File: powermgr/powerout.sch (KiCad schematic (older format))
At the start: 14 parts, among them IC2 AP24x1, IC3 AP24x1, IC4 AP24x1, IC5 AP24x1, IC6 AP24x1, IC7 AP24x1, IC8 AP24x1, IC9 AP24x1, J3 CONN_01X02, J4 CONN_01X02, P1 CONN_01X16

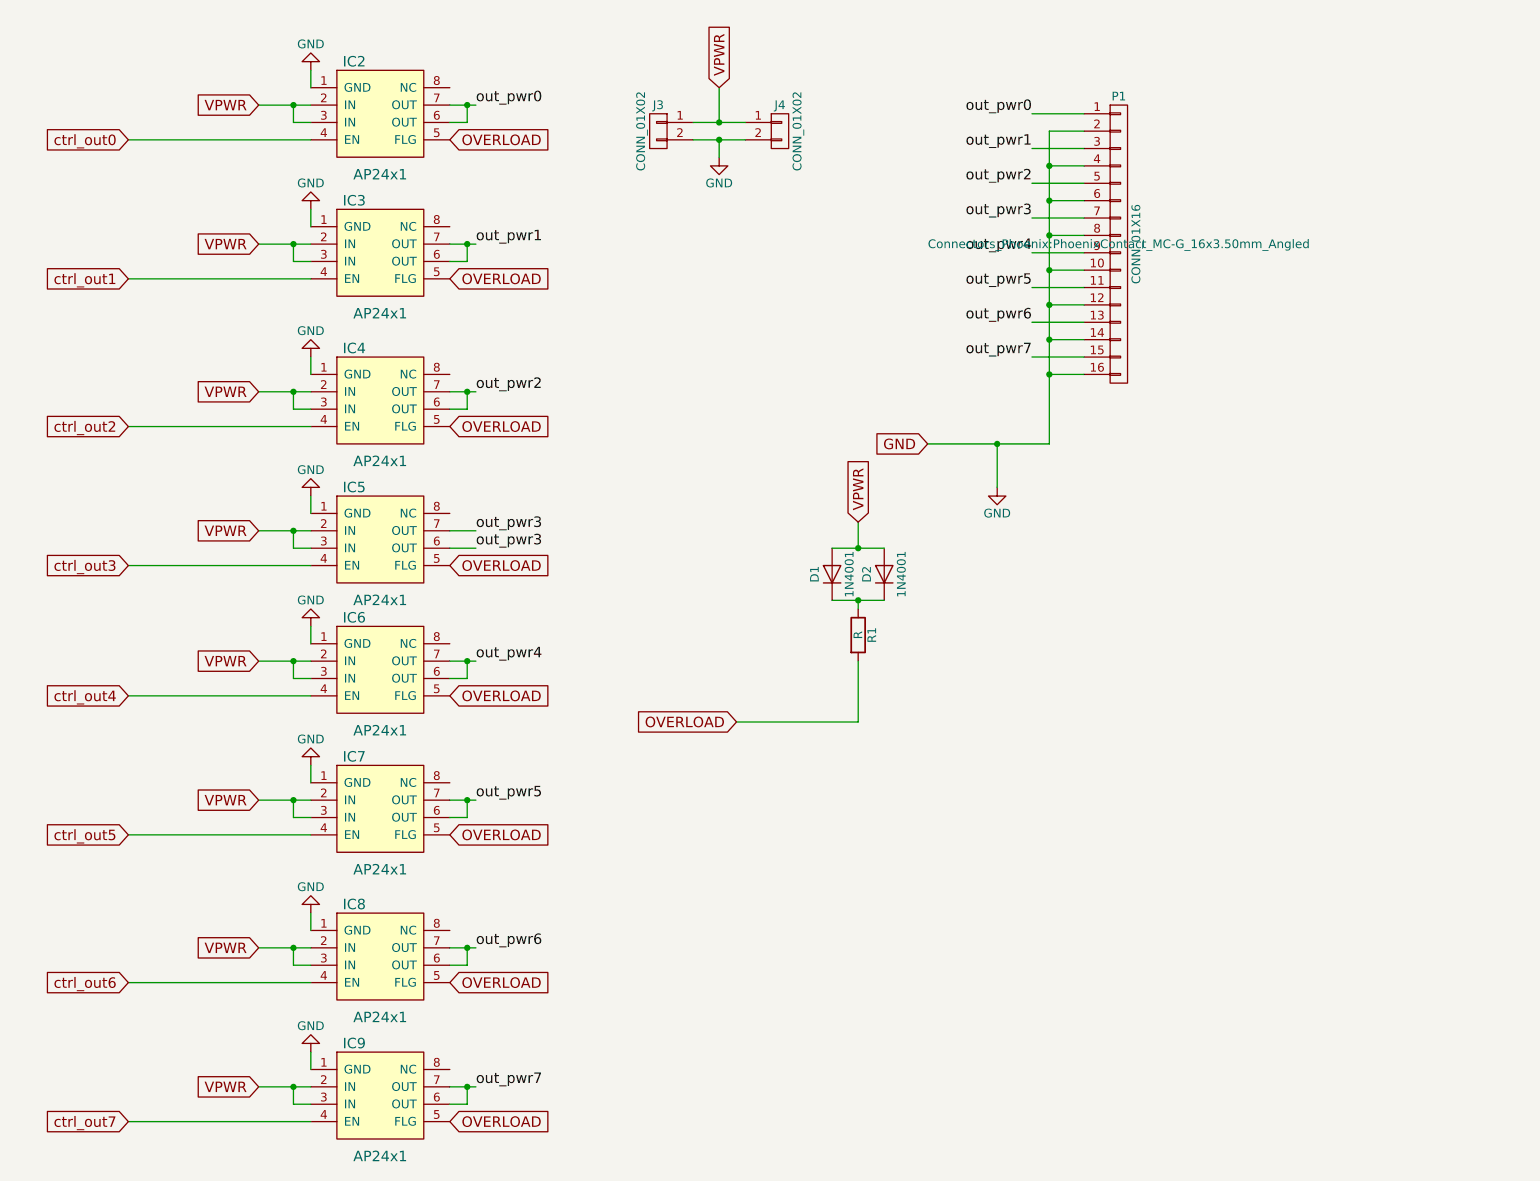
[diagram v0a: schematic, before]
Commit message: add LEDs and pulldowns
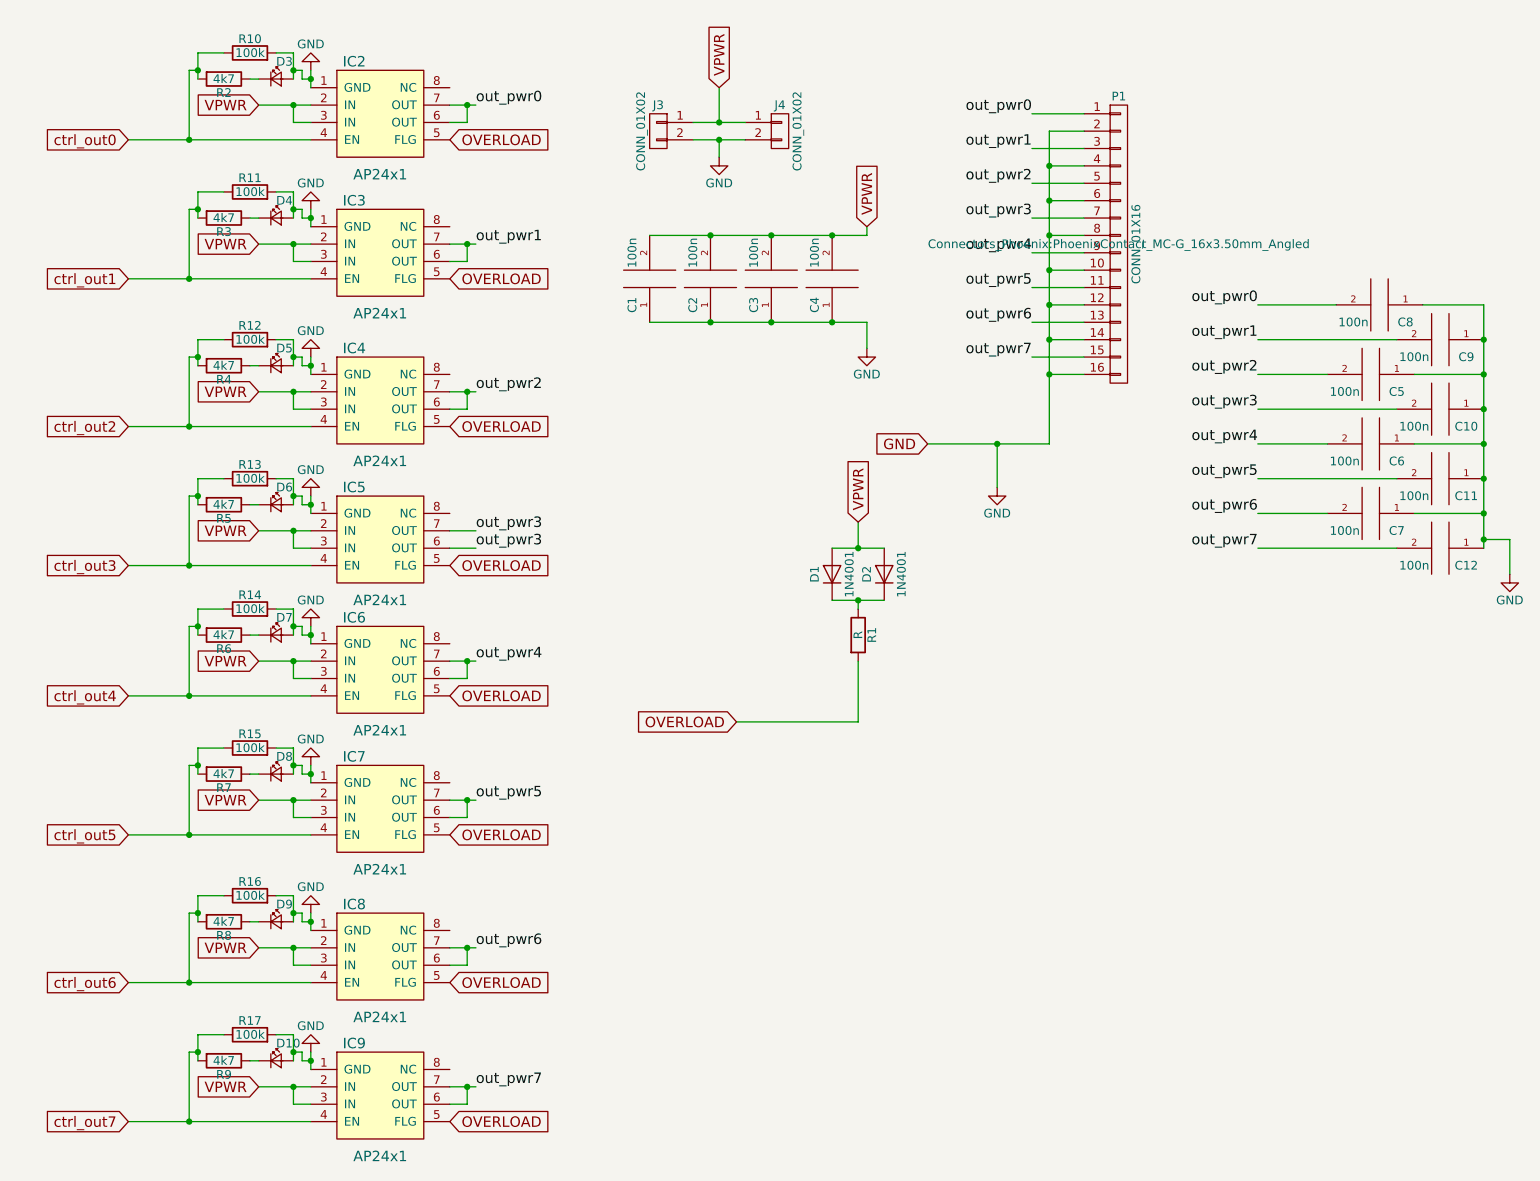
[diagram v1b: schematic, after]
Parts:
- added C1, C10, C11, C12, C2, C3, C4, C5, C6, C7, C8, C9: 100n, Capacitors_SMD:C_0805_HandSoldering, symbol CAP
- added D10, D3, D4, D5, D6, D7, D8, D9: LED_Small, LEDs:LED_0805, symbol LED_Small
- added R10, R11, R12, R13, R14, R15, R16, R17: 100k, Resistors_SMD:R_0805_HandSoldering, symbol R
- added R2, R3, R4, R5, R6, R7, R8, R9: 4k7, Resistors_SMD:R_0805_HandSoldering, symbol R
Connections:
- net GND: now also C1.1, C10.1, C11.1, C12.1, C2.1, C3.1, C4.1, C5.1, C6.1, C7.1, C8.1, C9.1, D10.2 (A), D3.2 (A), D4.2 (A), D5.2 (A), D6.2 (A), D7.2 (A), D8.2 (A), D9.2 (A), R10.2, R11.2, R12.2, R13.2, R14.2, R15.2, R16.2, R17.2
- net VPWR: now also C1.2, C2.2, C3.2, C4.2
- net ctrl_out0: now also R10.1, R2.2
- net ctrl_out1: now also R11.1, R3.2
- net ctrl_out2: now also R12.1, R4.2
- net ctrl_out3: now also R13.1, R5.2
- net ctrl_out4: now also R14.1, R6.2
- net ctrl_out5: now also R15.1, R7.2
- net ctrl_out6: now also R16.1, R8.2
- net ctrl_out7: now also R17.1, R9.2
- net out_pwr0: now also C8.2
- net out_pwr1: now also C9.2
- net out_pwr2: now also C5.2
- net out_pwr3: now also C10.2
- net out_pwr4: now also C6.2
- net out_pwr5: now also C11.2
- net out_pwr6: now also C7.2
- net out_pwr7: now also C12.2
- new net: D5.1 (K), R4.1
- new net: D4.1 (K), R3.1
- new net: D3.1 (K), R2.1
- new net: D6.1 (K), R5.1
- new net: D7.1 (K), R6.1
- new net: D8.1 (K), R7.1
- new net: D9.1 (K), R8.1
- new net: D10.1 (K), R9.1

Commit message: so-8 version, I bought wrong part number..
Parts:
- IC2, IC3, IC4, IC5, IC6, IC7, IC8, IC9: footprint Housings_SSOP:MSOP-8_3x3mm_Pitch0.65mm -> Housings_SOIC:SOIC-8_3.9x4.9mm_Pitch1.27mm
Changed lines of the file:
@@
 F 0 "IC2" H 2950 1250 60  0000 C CNN
 F 1 "AP24x1" H 3100 600 60  0000 C CNN
-F 2 "Housings_SSOP:MSOP-8_3x3mm_Pitch0.65mm" H 3150 900 60  0001 C CNN
+F 2 "Housings_SOIC:SOIC-8_3.9x4.9mm_Pitch1.27mm" H 3150 900 60  0001 C CNN
 F 3 "" H 3150 900 60  0000 C CNN
 F 4 "Diodes Incorporated" H 3100 500 60  0001 C CNN "Manufacturer"
@@
 F 0 "IC3" H 2950 2050 60  0000 C CNN
 F 1 "AP24x1" H 3100 1400 60  0000 C CNN
-F 2 "Housings_SSOP:MSOP-8_3x3mm_Pitch0.65mm" H 3150 1700 60  0001 C CNN
+F 2 "Housings_SOIC:SOIC-8_3.9x4.9mm_Pitch1.27mm" H 3150 1700 60  0001 C CNN
 F 3 "" H 3150 1700 60  0000 C CNN
 F 4 "Diodes Incorporated" H 3100 1300 60  0001 C CNN "Manufacturer"
@@
 F 0 "IC4" H 2950 2900 60  0000 C CNN
 F 1 "AP24x1" H 3100 2250 60  0000 C CNN
-F 2 "Housings_SSOP:MSOP-8_3x3mm_Pitch0.65mm" H 3150 2550 60  0001 C CNN
+F 2 "Housings_SOIC:SOIC-8_3.9x4.9mm_Pitch1.27mm" H 3150 2550 60  0001 C CNN
 F 3 "" H 3150 2550 60  0000 C CNN
 F 4 "Diodes Incorporated" H 3100 2150 60  0001 C CNN "Manufacturer"
@@
 F 0 "IC5" H 2950 3700 60  0000 C CNN
 F 1 "AP24x1" H 3100 3050 60  0000 C CNN
-F 2 "Housings_SSOP:MSOP-8_3x3mm_Pitch0.65mm" H 3150 3350 60  0001 C CNN
+F 2 "Housings_SOIC:SOIC-8_3.9x4.9mm_Pitch1.27mm" H 3150 3350 60  0001 C CNN
 F 3 "" H 3150 3350 60  0000 C CNN
 F 4 "Diodes Incorporated" H 3100 2950 60  0001 C CNN "Manufacturer"
@@
 F 0 "IC6" H 2950 4450 60  0000 C CNN
 F 1 "AP24x1" H 3100 3800 60  0000 C CNN
-F 2 "Housings_SSOP:MSOP-8_3x3mm_Pitch0.65mm" H 3150 4100 60  0001 C CNN
+F 2 "Housings_SOIC:SOIC-8_3.9x4.9mm_Pitch1.27mm" H 3150 4100 60  0001 C CNN
 F 3 "" H 3150 4100 60  0000 C CNN
 F 4 "Diodes Incorporated" H 3100 3700 60  0001 C CNN "Manufacturer"
@@
 F 0 "IC7" H 2950 5250 60  0000 C CNN
 F 1 "AP24x1" H 3100 4600 60  0000 C CNN
-F 2 "Housings_SSOP:MSOP-8_3x3mm_Pitch0.65mm" H 3150 4900 60  0001 C CNN
+F 2 "Housings_SOIC:SOIC-8_3.9x4.9mm_Pitch1.27mm" H 3150 4900 60  0001 C CNN
 F 3 "" H 3150 4900 60  0000 C CNN
 F 4 "Diodes Incorporated" H 3100 4500 60  0001 C CNN "Manufacturer"
@@
 F 0 "IC8" H 2950 6100 60  0000 C CNN
 F 1 "AP24x1" H 3100 5450 60  0000 C CNN
-F 2 "Housings_SSOP:MSOP-8_3x3mm_Pitch0.65mm" H 3150 5750 60  0001 C CNN
+F 2 "Housings_SOIC:SOIC-8_3.9x4.9mm_Pitch1.27mm" H 3150 5750 60  0001 C CNN
 F 3 "" H 3150 5750 60  0000 C CNN
 F 4 "Diodes Incorporated" H 3100 5350 60  0001 C CNN "Manufacturer"
@@
 F 0 "IC9" H 2950 6900 60  0000 C CNN
 F 1 "AP24x1" H 3100 6250 60  0000 C CNN
-F 2 "Housings_SSOP:MSOP-8_3x3mm_Pitch0.65mm" H 3150 6550 60  0001 C CNN
+F 2 "Housings_SOIC:SOIC-8_3.9x4.9mm_Pitch1.27mm" H 3150 6550 60  0001 C CNN
 F 3 "" H 3150 6550 60  0000 C CNN
 F 4 "Diodes Incorporated" H 3100 6150 60  0001 C CNN "Manufacturer"

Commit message: fixups and text
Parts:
- P1: value CONN_01X16 -> PWR_OUT
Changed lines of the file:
@@
 P 7350 1700
 F 0 "P1" H 7350 2550 50  0000 C CNN
-F 1 "CONN_01X16" V 7450 1700 50  0000 C CNN
+F 1 "PWR_OUT" V 7450 1700 50  0000 C CNN
 F 2 "Connectors_Phoenix:PhoenixContact_MC-G_16x3.50mm_Angled" H 7350 1700 50  0000 C CNN
 F 3 "" H 7350 1700 50  0000 C CNN
@@
 VPWR
 $Comp
-L GND #PWR07
+L GND #PWR09
 U 1 1 5908E164
 P 6650 3100
-F 0 "#PWR07" H 6650 2850 50  0001 C CNN
+F 0 "#PWR09" H 6650 2850 50  0001 C CNN
 F 1 "GND" H 6650 2950 50  0000 C CNN
 F 2 "" H 6650 3100 50  0001 C CNN
@@
 $EndComp
 $Comp
-L GND #PWR08
+L GND #PWR010
 U 1 1 5908E298
 P 2700 3150
-F 0 "#PWR08" H 2700 2900 50  0001 C CNN
+F 0 "#PWR010" H 2700 2900 50  0001 C CNN
 F 1 "GND" H 2700 3000 50  0000 C CNN
 F 2 "" H 2700 3150 50  0001 C CNN
@@
 $EndComp
 $Comp
-L GND #PWR09
+L GND #PWR011
 U 1 1 5908E35C
 P 2700 3900
-F 0 "#PWR09" H 2700 3650 50  0001 C CNN
+F 0 "#PWR011" H 2700 3650 50  0001 C CNN
 F 1 "GND" H 2700 3750 50  0000 C CNN
 F 2 "" H 2700 3900 50  0001 C CNN
@@
 $EndComp
 $Comp
-L GND #PWR010
+L GND #PWR012
 U 1 1 5908E706
 P 2700 4700
-F 0 "#PWR010" H 2700 4450 50  0001 C CNN
+F 0 "#PWR012" H 2700 4450 50  0001 C CNN
 F 1 "GND" H 2700 4550 50  0000 C CNN
 F 2 "" H 2700 4700 50  0001 C CNN
@@
 $EndComp
 $Comp
-L GND #PWR011
+L GND #PWR013
 U 1 1 5908E72C
 P 2700 5550
-F 0 "#PWR011" H 2700 5300 50  0001 C CNN
+F 0 "#PWR013" H 2700 5300 50  0001 C CNN
 F 1 "GND" H 2700 5400 50  0000 C CNN
 F 2 "" H 2700 5550 50  0001 C CNN
@@
 $EndComp
 $Comp
-L GND #PWR012
+L GND #PWR014
 U 1 1 5908E7A5
 P 2700 6350
-F 0 "#PWR012" H 2700 6100 50  0001 C CNN
+F 0 "#PWR014" H 2700 6100 50  0001 C CNN
 F 1 "GND" H 2700 6200 50  0000 C CNN
 F 2 "" H 2700 6350 50  0001 C CNN
@@
 $EndComp
 $Comp
-L GND #PWR013
+L GND #PWR015
 U 1 1 5908EAFD
 P 2700 2350
-F 0 "#PWR013" H 2700 2100 50  0001 C CNN
+F 0 "#PWR015" H 2700 2100 50  0001 C CNN
 F 1 "GND" H 2700 2200 50  0000 C CNN
 F 2 "" H 2700 2350 50  0001 C CNN
@@
 $EndComp
 $Comp
-L GND #PWR014
+L GND #PWR016
 U 1 1 5908EDCF
 P 2700 1500
-F 0 "#PWR014" H 2700 1250 50  0001 C CNN
+F 0 "#PWR016" H 2700 1250 50  0001 C CNN
 F 1 "GND" H 2700 1350 50  0000 C CNN
 F 2 "" H 2700 1500 50  0001 C CNN
@@
 $EndComp
 $Comp
-L GND #PWR015
+L GND #PWR017
 U 1 1 5908EDF5
 P 2700 700
-F 0 "#PWR015" H 2700 450 50  0001 C CNN
+F 0 "#PWR017" H 2700 450 50  0001 C CNN
 F 1 "GND" H 2700 550 50  0000 C CNN
 F 2 "" H 2700 700 50  0001 C CNN
@@
 $EndComp
 $Comp
-L GND #PWR016
+L GND #PWR018
 U 1 1 590BC83B
 P 5050 1200
-F 0 "#PWR016" H 5050 950 50  0001 C CNN
+F 0 "#PWR018" H 5050 950 50  0001 C CNN
 F 1 "GND" H 5050 1050 50  0000 C CNN
 F 2 "" H 5050 1200 50  0001 C CNN
@@
 $EndComp
 $Comp
-L GND #PWR017
+L GND #PWR019
 U 1 1 59475ECA
 P 9600 3600
-F 0 "#PWR017" H 9600 3350 50  0001 C CNN
+F 0 "#PWR019" H 9600 3350 50  0001 C CNN
 F 1 "GND" H 9600 3450 50  0000 C CNN
 F 2 "" H 9600 3600 50  0001 C CNN
@@
 $EndComp
 $Comp
-L GND #PWR018
+L GND #PWR020
 U 1 1 5947C358
 P 5900 2300
-F 0 "#PWR018" H 5900 2050 50  0001 C CNN
+F 0 "#PWR020" H 5900 2050 50  0001 C CNN
 F 1 "GND" H 5900 2150 50  0000 C CNN
 F 2 "" H 5900 2300 50  0001 C CNN
